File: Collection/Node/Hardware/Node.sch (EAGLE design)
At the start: 13 parts, among them IC1 4050D, IC2 LP298XS, IC3 DS3231/SO, M2 WIRELESS-NRF24L01-PA-EXT, U2 ATMEGA328P-PU, X1 MICROSD

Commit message: Updated schematic
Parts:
- added C1, C2, C3, C4: 22pF, rcl:C-US050-035X075
- added Q1: 16MHz, crystal:CRYSTALHC49S
- added R2: 10K, rcl:R-US_R0805
- added SW2: FSMSM, Switch:FSMSM
- R3, R4: value (none) -> 10K
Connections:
- new net N$6: R2.1, SW2.1, U2.PC6(PCINT14/!RESET)
- new net N$7: C1.1, Q1.1, U2.(PCINT7/XTAL2/TOSC2)PB7
- new net N$8: C2.1, Q1.2, U2.(PCINT6/XTAL1/TOSC1)PB6
- net +3V3: now also C4.1
- net +5V: now also C3.1, R2.2, U2.AVCC
- net GND: now also C1.2, C2.2, C3.2, C4.2, SW2.2, U2.AREF, U2.GND1
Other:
- moved on the sheet: R3, R4

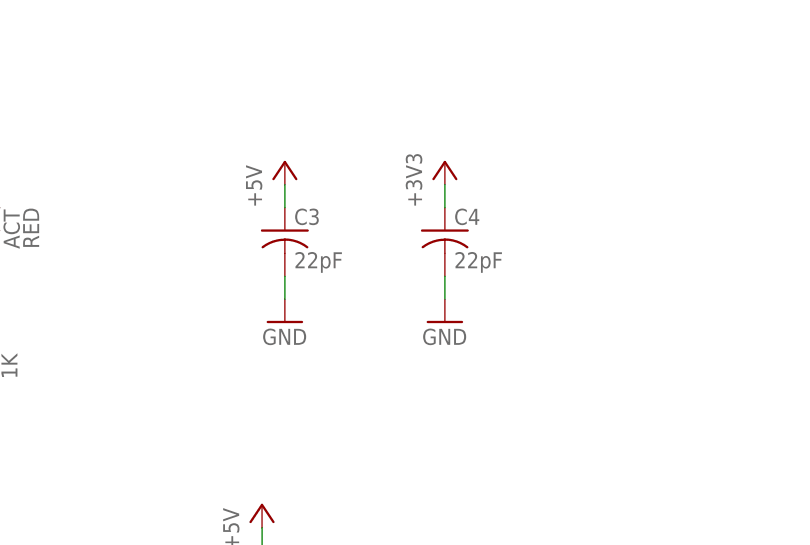
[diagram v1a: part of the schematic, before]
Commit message: Adjusted board size
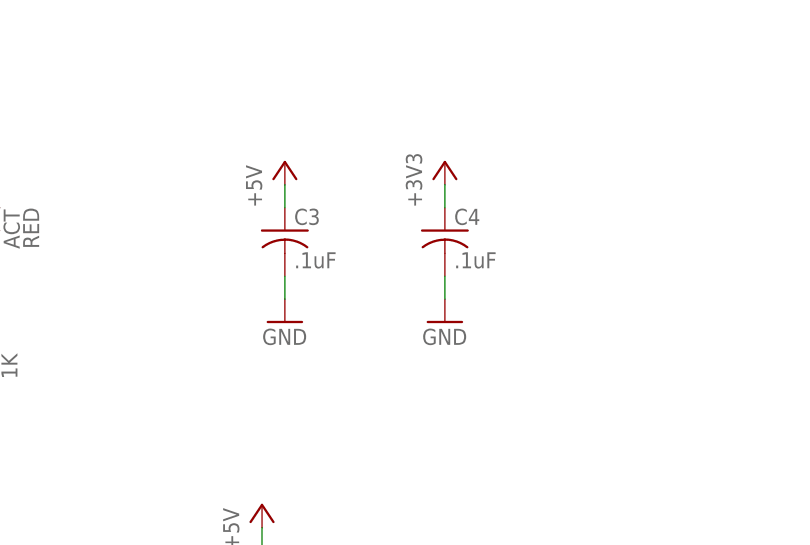
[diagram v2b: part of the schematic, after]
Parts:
- C3, C4: value 22pF -> .1uF
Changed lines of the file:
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@@
 <part name="Q1" library="crystal" library_urn="urn:adsk.eagle:library:204" deviceset="CRYSTAL" device="HC49S" package3d_urn="urn:adsk.eagle:package:12071/1" value="16MHz"/>
 <part name="GND8" library="supply1" library_urn="urn:adsk.eagle:library:371" deviceset="GND" device=""/>
-<part name="C3" library="rcl" library_urn="urn:adsk.eagle:library:334" deviceset="C-US" device="050-035X075" package3d_urn="urn:adsk.eagle:package:23677/1" value="22pF"/>
-<part name="C4" library="rcl" library_urn="urn:adsk.eagle:library:334" deviceset="C-US" device="050-035X075" package3d_urn="urn:adsk.eagle:package:23677/1" value="22pF"/>
+<part name="C3" library="rcl" library_urn="urn:adsk.eagle:library:334" deviceset="C-US" device="050-035X075" package3d_urn="urn:adsk.eagle:package:23677/1" value=".1uF"/>
+<part name="C4" library="rcl" library_urn="urn:adsk.eagle:library:334" deviceset="C-US" device="050-035X075" package3d_urn="urn:adsk.eagle:package:23677/1" value=".1uF"/>
 <part name="P+5" library="supply1" library_urn="urn:adsk.eagle:library:371" deviceset="+5V" device=""/>
 <part name="+3V4" library="supply1" deviceset="+3V3" device=""/>

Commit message: updated schematic
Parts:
- removed ACT: RED, adafruit:LEDCHIP-LED0805
- removed B1: CR1220, microbuilder:BATTERYCR1220_SMT
- removed J2: (no value), SparkFun-Connectors:CONN_02JST-PTH-2
- removed J3: (no value), SparkFun-Connectors:CONN_04JST-PTH
- removed X1: MICROSD, adafruit:MICROSD
- added BT1: KEYSTONE_ELECTRONICS_3034KEYSTONE_ELECTRONICS_3034_0_0, Keystone Electronics - 3034:KEYSTONE_ELECTRONICS_3034KEYSTONE_ELECTRONICS_3034_0_0
- added H1, H2: MOUNT-PAD-ROUND3.0, holes:MOUNT-PAD-ROUND3.0
- added JP1, JP3: (no value), pinhead:PINHD-1X2
- added JP2: (no value), pinhead:PINHD-1X4
- added LED1: RED, led:LEDCHIPLED_0805
- added LED2: GREEN, led:LEDCHIPLED_0805
- added LED3: Yellow, led:LEDCHIPLED_0805
- added R5, R6: 1K, rcl:R-US_R0805
- added U$1: 1051620001A, Molex_micro_SD:1051620001A
- C1, C2, C3, C4: device rcl:C-US050-035X075 -> rcl:C-USC0805
- Q1: device crystal:CRYSTALHC49S -> special:XTAL/S
- R1: device adafruit:R-US_R0805 -> rcl:R-US_R0805
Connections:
- removed net CD: X1.CARD_DETECT
- removed net GND_SD: IC1E.I, IC1F.I, IC1P.VSS
- removed net V_EXTERNAL_BATTERY: J2.2
- new net N$10: LED2.A, R5.1
- new net N$11: LED3.A, R6.1
- new net N$12: R6.2, U2.(PCINT22/OC0A/AIN0)PD6
- new net N$9: R5.2, U2.(PCINT21/OC0B/T1)PD5
- new net V_PACK: JP1.1
- net +3V3: now also U$1.VDD; no longer X1.VDD
- net +5V: now also JP2.4; no longer J3.1
- net DO: now also U$1.DAT0; no longer X1.DATA_OUT
- net GND: now also BT1.CATHODE, IC1E.I, IC1F.I, IC1P.VSS, JP1.2, JP2.3, JP3.2, LED2.C, LED3.C, U$1.GND, U$1.GND@1, U$1.GND@2, U$1.GND@3, U$1.VSS; no longer B1.-, J2.1, J3.2, X1.GND, X1.GND1, X1.VSS
- net N$1: now also LED1.A; no longer ACT.A
- net N$2: now also U$1.CLK; no longer X1.SCLK
- net N$3: now also U$1.CD/DAT3; no longer X1.CS
- net N$4: now also LED1.C; no longer ACT.C
- net N$5: now also U$1.CMD; no longer X1.DATA_IN
- net SCL: now also JP2.2; no longer J3.3
- net SDA: now also JP2.1; no longer J3.4
- net VBAT: now also BT1.ANODE; no longer B1.+
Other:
- moved on the sheet: IC2, IC3
